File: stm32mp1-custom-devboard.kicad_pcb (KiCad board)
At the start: 2 copper layers, 120 x 72 mm, 16 parts, among them Con1 52746-0671, Con2 505110-2491, P1 FH12A-30S-0.5SH(55), U1 TPS61169DCKR, U2 MCP1703T-3302E

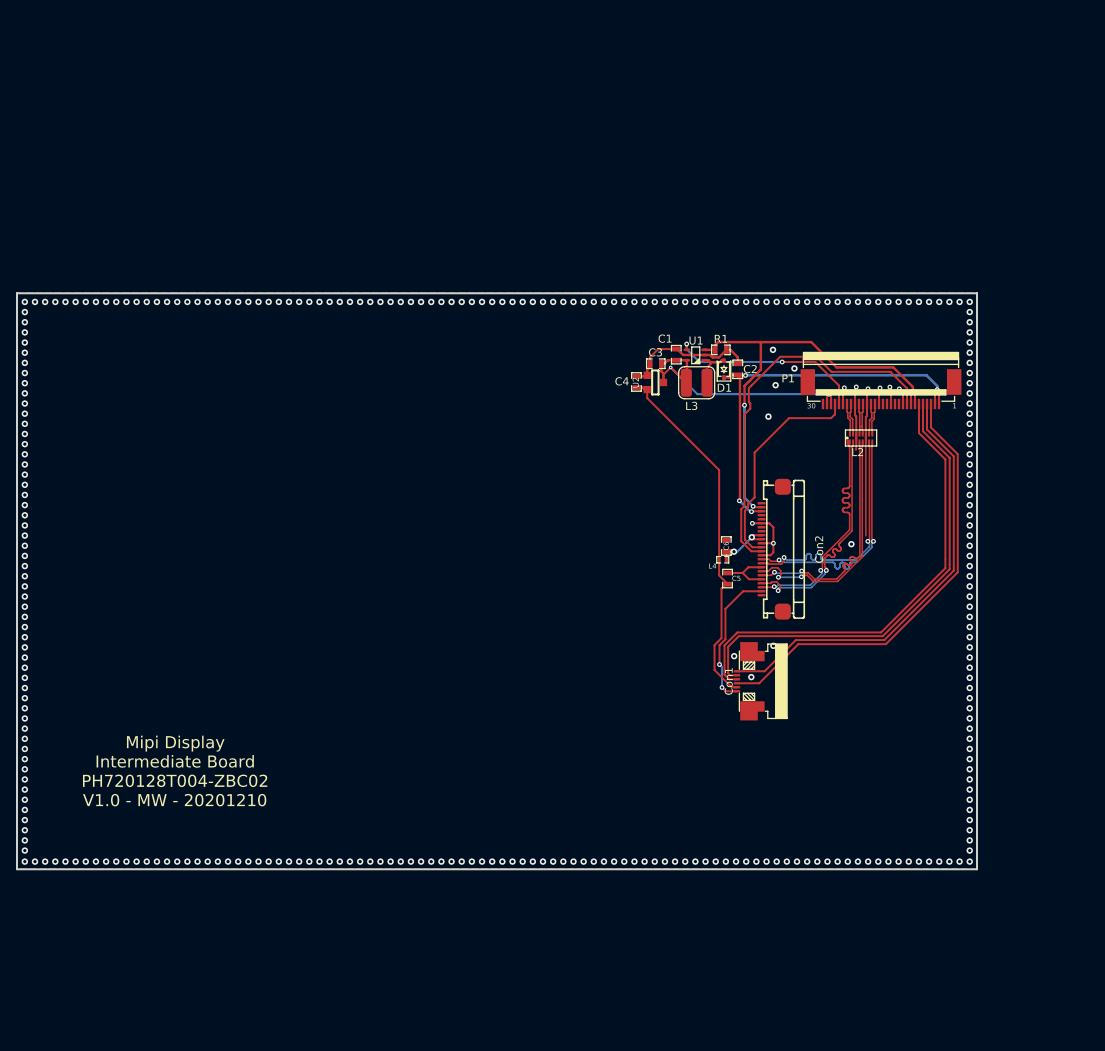
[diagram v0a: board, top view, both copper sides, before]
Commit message: Added stm32mp1 module and arduino shield
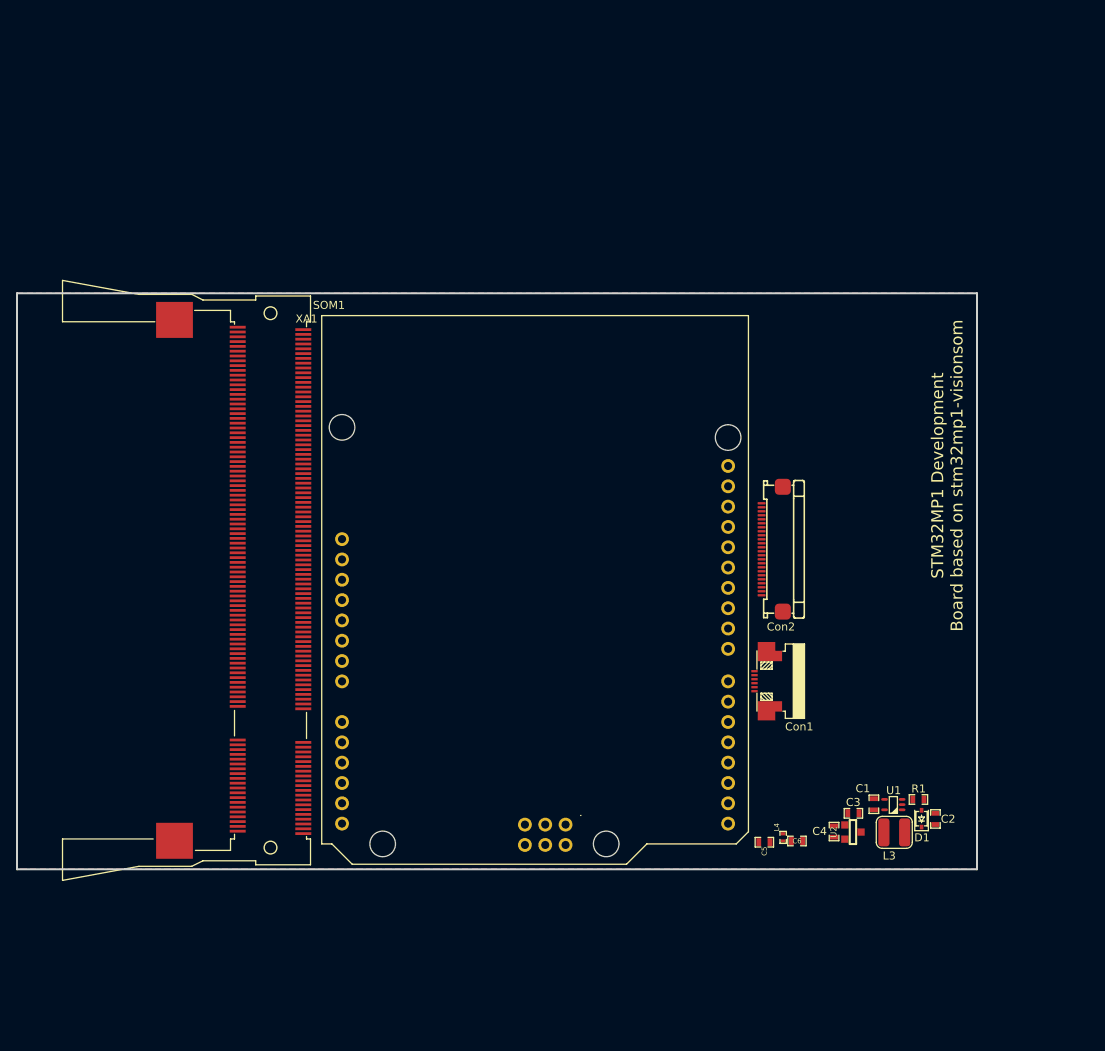
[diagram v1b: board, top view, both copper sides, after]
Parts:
- removed L2: EMI8133MUTAG, Inductors:EMI8133MUTAG
- removed P1: FH12A-30S-0.5SH(55), Fpc_Connectors:FH12A-30S-0.5SH
- added SOM1: VisionSOM-STM32MP1, SomLabs_SOM:VisionSOM-STM32MP1, F.Cu at (124.8, 102.3)
- added XA1: Arduino_101_Shield, Arduino:Arduino_101_Shield, F.Cu at (131.2, 69.2)
- moved D1 61.4 mm to (206.2, 132.1)
- moved U2 61.4 mm to (197.6, 133.8)
- moved C1 61.4 mm to (200.2, 130.3)
- moved C2 61.4 mm to (207.9, 132.1)
- moved C4 61.4 mm to (195.2, 133.7)
- moved L3 61.4 mm to (202.8, 133.8)
- moved R1 61.4 mm to (205.8, 129.7)
- moved U1 61.4 mm to (202.7, 130.3)
- moved C3 61.4 mm to (197.7, 131.4)
- moved C6 37.9 mm to (190.6, 134.9), turned to 0 degrees
- moved L4 35.5 mm to (188.9, 134.4), turned to 90 degrees
- moved C5 33.3 mm to (186.5, 135.0), turned to 0 degrees
- moved Con1 2.19 mm to (187.3, 114.9)
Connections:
- Con1 pad 3: /LCD+Touchscreen common connector/TP_NT -> (no net)
- Con1 pad 4: /LCD+Touchscreen common connector/TP_SDA -> (no net)
- Con1 pad 5: /LCD+Touchscreen common connector/TP_SCL -> (no net)
- Con1 pad 6: /LCD+Touchscreen common connector/TP_RESET -> (no net)
- Con2 pad 12: /LCD+Touchscreen common connector/LCD_RESET -> (no net)
- Con2 pad 13: /LCD+Touchscreen common connector/LCD_TE -> (no net)
- Con2 pad 15: /LCD+Touchscreen/MIPI_CLK+ -> (no net)
- Con2 pad 16: /LCD+Touchscreen/MIPI_CLK- -> (no net)
- Con2 pad 18: /LCD+Touchscreen/MIPI_D1+ -> (no net)
- Con2 pad 19: /LCD+Touchscreen/MIPI_D1- -> (no net)
- Con2 pad 21: /LCD+Touchscreen/MIPI_D0+ -> (no net)
- Con2 pad 22: /LCD+Touchscreen/MIPI_D0- -> (no net)
- U1 pad 4: /LCD+Touchscreen common connector/LCD_BACKLIGHT_PWM -> (no net)
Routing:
- net GND: track 86.2 -> 0.00 mm, vias 314 -> 0
- net /LCD+Touchscreen/LCD_LED-: track 81.2 -> 0.00 mm, vias 3 -> 0
- net /LCD+Touchscreen common connector/TP_SDA: track 59.0 -> 0.00 mm
- net /LCD+Touchscreen common connector/TP_SCL: track 58.3 -> 0.00 mm
- net /LCD+Touchscreen common connector/TP_NT: track 55.8 -> 0.00 mm
- net /LCD+Touchscreen common connector/TP_RESET: track 54.5 -> 0.00 mm
- net /LCD+Touchscreen/LCD_LED+: track 51.5 -> 0.00 mm, vias 4 -> 0
- net /LCD+Touchscreen common connector/LCD_TE: track 47.7 -> 0.00 mm
- net /LCD+Touchscreen/Touchscreen Power Supply/VOUT_3.3V_250mA: track 45.2 -> 0.00 mm
- net VDD: track 37.5 -> 0.00 mm, vias 2 -> 0
- net /LCD+Touchscreen/MIPI_CLK-: track 30.4 -> 0.00 mm, vias 2 -> 0
- net /LCD+Touchscreen/MIPI_CLK+: track 30.4 -> 0.00 mm, vias 2 -> 0
- net /LCD+Touchscreen/MIPI_D1-: track 30.2 -> 0.00 mm, vias 2 -> 0
- net /LCD+Touchscreen/MIPI_D0+: track 30.2 -> 0.00 mm, vias 2 -> 0
- net /LCD+Touchscreen/MIPI_D1+: track 30.2 -> 0.00 mm, vias 2 -> 0
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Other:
- board text added: "STM32MP1 Development Board based on stm32mp1-visionsom"
- board text removed: "Mipi Display Intermediate Board PH720128T004-ZBC02 V1.0 - MW - 20201210"

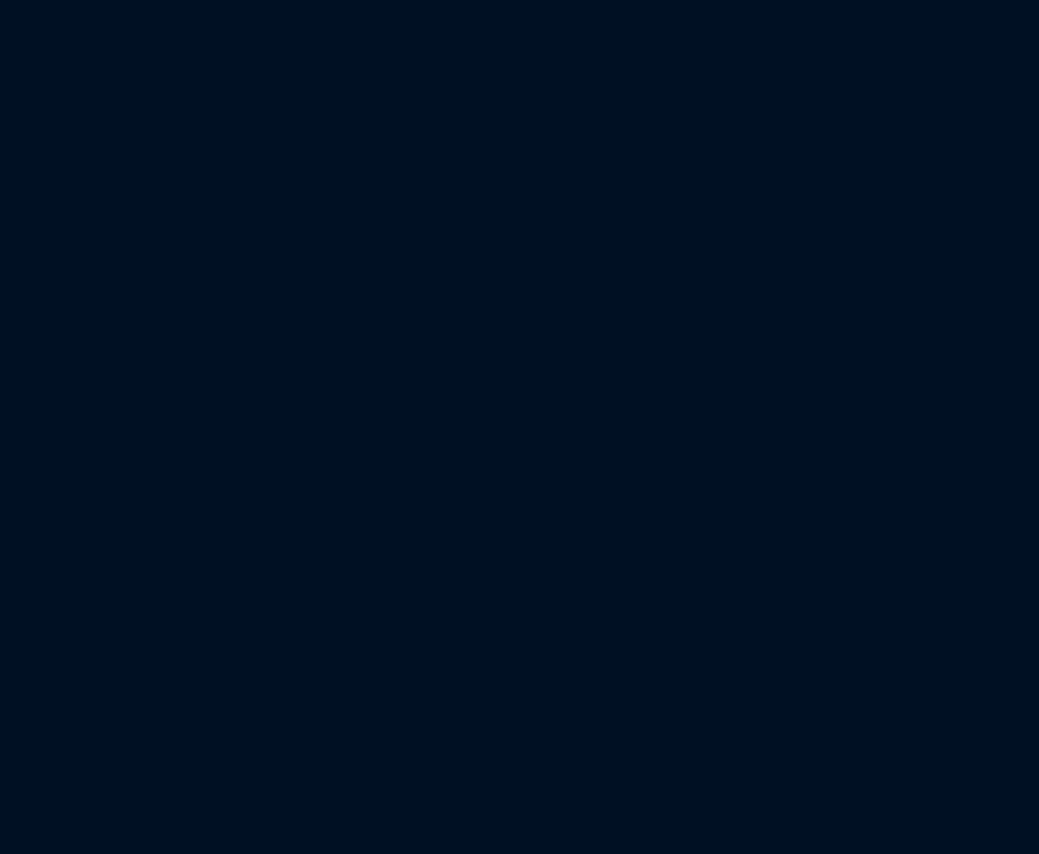
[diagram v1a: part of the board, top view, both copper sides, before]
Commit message: Added new components and hierarchical sheets
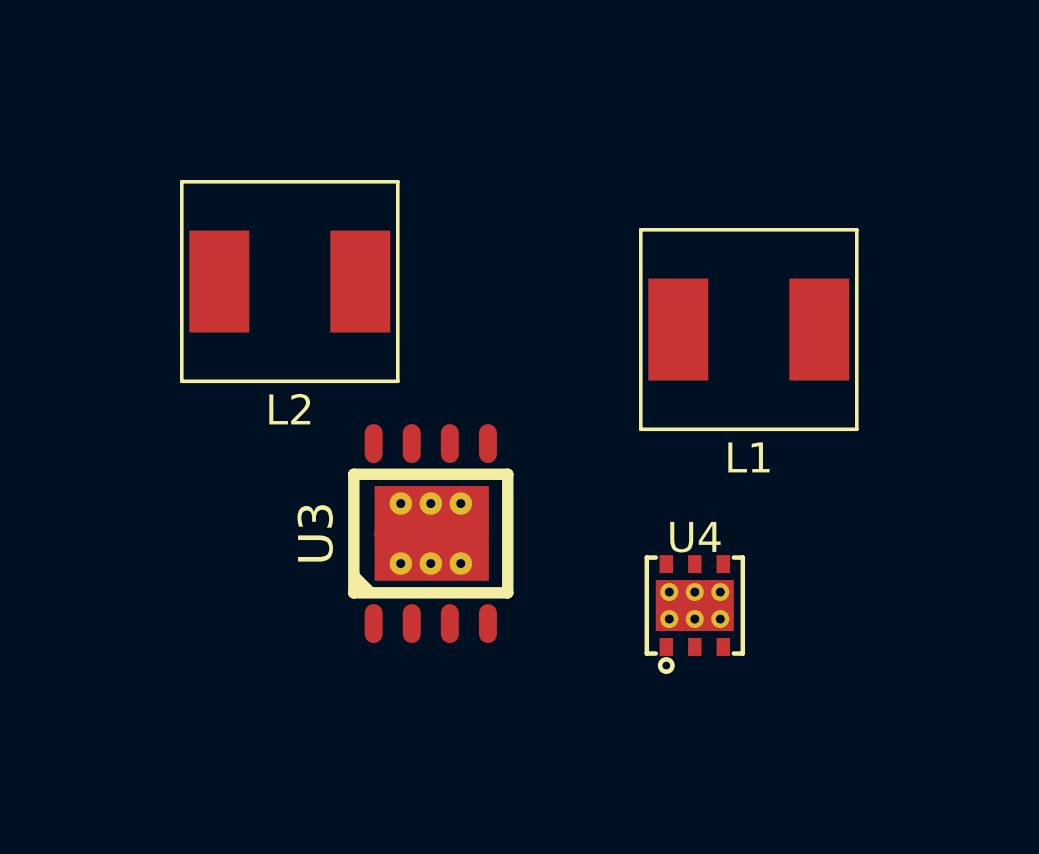
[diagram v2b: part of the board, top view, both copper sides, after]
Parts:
- added L1: 3.3uH-13.5A-ASPI-0630HI-3R3M-T15, Inductors:ASPI-0630HI-3R3M-T15, F.Cu at (163.4, 112.9)
- added L2: 3.3uH-13.5A-ASPI-0630HI-3R3M-T15, Inductors:ASPI-0630HI-3R3M-T15, F.Cu at (148.1, 111.3)
- added U3: ST1S10PHR, Switching:ST1S10PHR_SOIC8, F.Cu at (152.8, 119.7)
- added U4: ST1S09IPUR, Switching:ST1S09IPUR, F.Cu at (161.6, 122.1)
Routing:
- added copper zone on In2.Cu, net GND
- added copper zone on In1.Cu, net VDD
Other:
- copper layers 2 -> 4

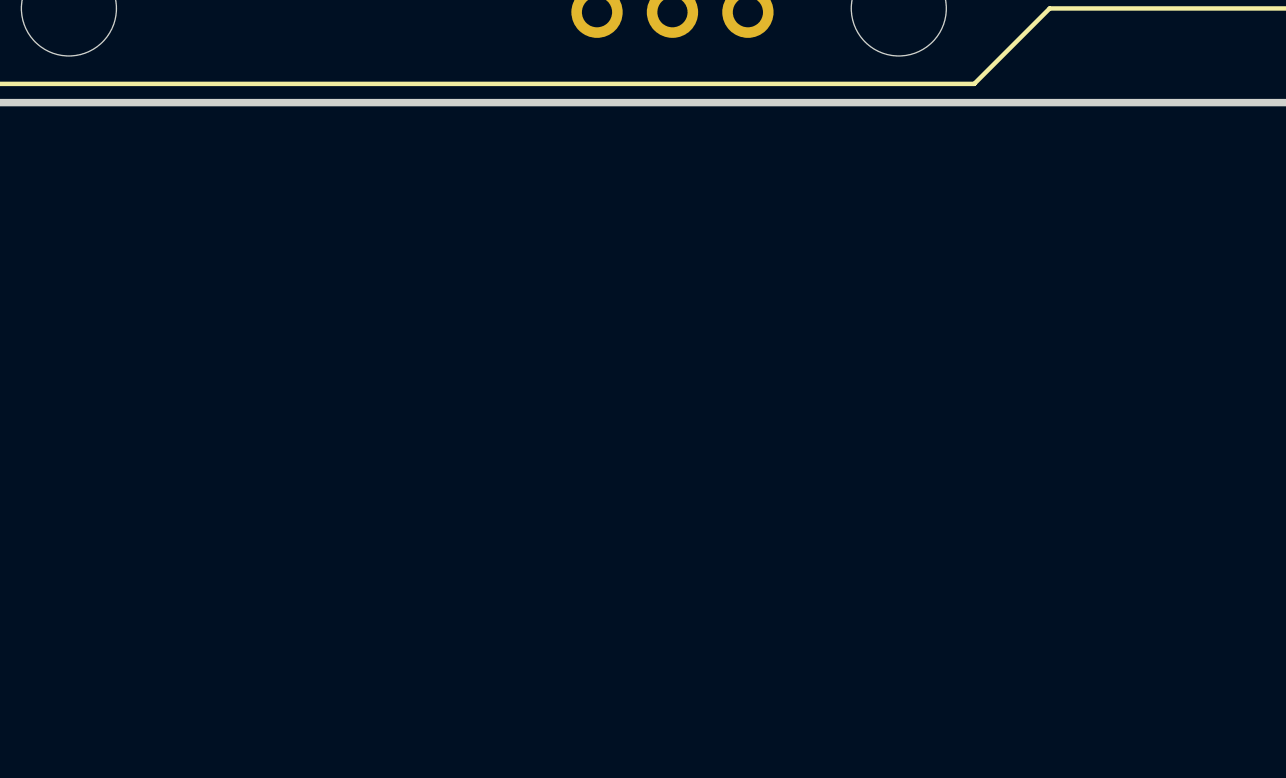
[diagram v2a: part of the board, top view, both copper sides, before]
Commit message: Added power source module
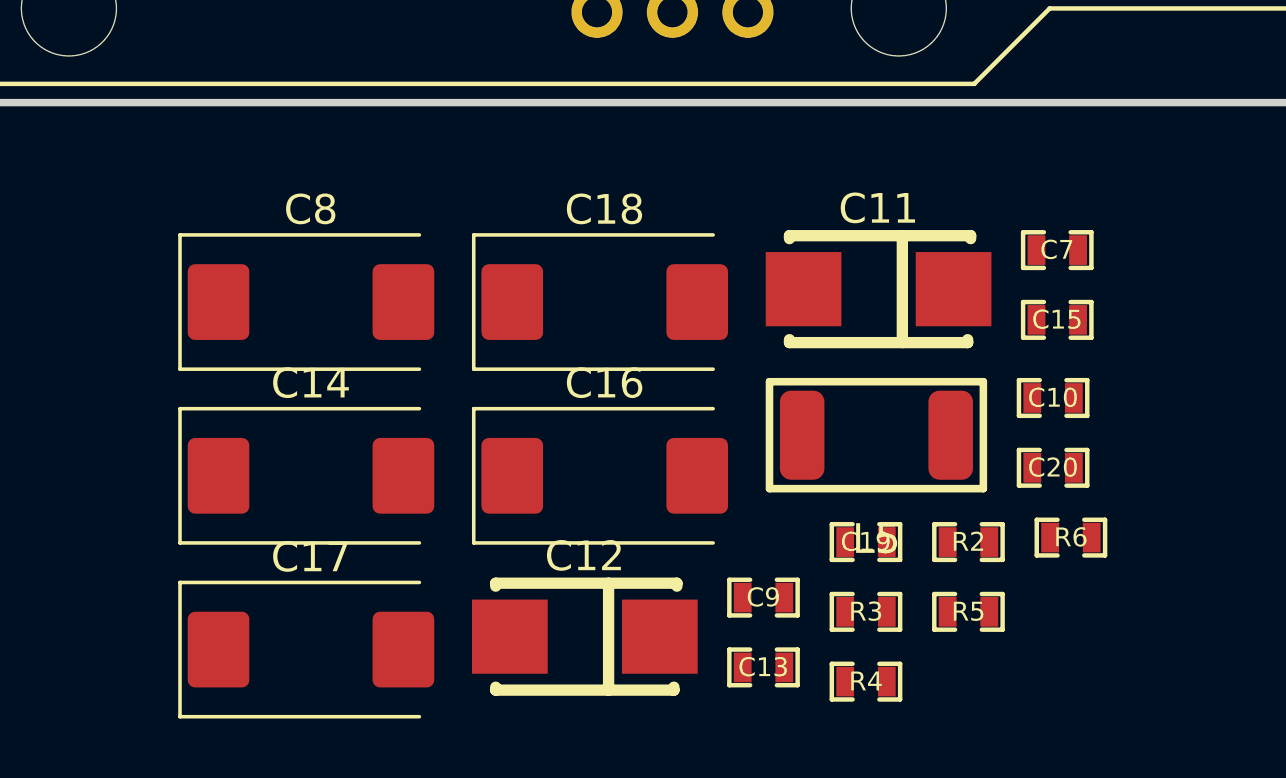
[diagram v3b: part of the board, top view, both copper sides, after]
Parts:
- added C10: 100nF/50V, Capacitors_Smd_0603:100nF_0603, F.Cu at (172.0, 148.4)
- added C11: 10uF/35V, Smd_Tantal:10uF_35V_C, F.Cu at (166.1, 144.7)
- added C12: 10uF/35V, Smd_Tantal:10uF_35V_C, F.Cu at (156.2, 156.4)
- added C13: 100nF/50V, Capacitors_Smd_0603:100nF_0603, F.Cu at (162.2, 157.4)
- added C14: 22uF35V, Smd_Tantal:22uF_35V_Size_D, F.Cu at (147.0, 151.0)
- added C15: 10nF/50V, Capacitors_Smd_0603:10nF_0603, F.Cu at (172.1, 145.7)
- added C16: 22uF35V, Smd_Tantal:22uF_35V_Size_D, F.Cu at (156.9, 151.0)
- added C17: 22uF35V, Smd_Tantal:22uF_35V_Size_D, F.Cu at (147.0, 156.8)
- added C18: 22uF35V, Smd_Tantal:22uF_35V_Size_D, F.Cu at (156.9, 145.1)
- added C19: 100nF/50V, Capacitors_Smd_0603:100nF_0603, F.Cu at (165.7, 153.2)
- added C20: 100nF/50V, Capacitors_Smd_0603:100nF_0603, F.Cu at (172.0, 150.7)
- added C7: 100nF/50V, Capacitors_Smd_0603:100nF_0603, F.Cu at (172.1, 143.4)
- added C8: 22uF35V, Smd_Tantal:22uF_35V_Size_D, F.Cu at (147.0, 145.1)
- added C9: 100nF/50V, Capacitors_Smd_0603:100nF_0603, F.Cu at (162.2, 155.1)
- added L5: 742792515, Inductors:742792515, F.Cu at (166.0, 149.6)
- added R2: 2k,1%, Resistor_Smd_0603:2k_0603, F.Cu at (169.1, 153.2)
- added R3: 68k, Resistor_Smd_0603:68k_0603, F.Cu at (165.7, 155.6)
- added R4: 21k, Resistor_Smd_0603:21k_0603, F.Cu at (165.7, 157.9)
- added R5: 11k,1%, Resistor_Smd_0603:11k_0603, F.Cu at (169.1, 155.6)
- added R6: 2k,1%, Resistor_Smd_0603:2k_0603, F.Cu at (172.6, 153.1)
- L1, L2: value 3.3uH-13.5A-ASPI-0630HI-3R3M-T15 -> 3.3uH-13.5A
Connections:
- L1 pad 1: (no net) -> Net-(L1-Pad1)
- L1 pad 2: (no net) -> /Power Supply Module/POWER_OUT_5V_3A
- L2 pad 1: (no net) -> Net-(L2-Pad1)
- L2 pad 2: (no net) -> /Power Supply Module/POWER_OUT_3V3_2A
- U3 pad 0: Net-(U3-Pad0) -> GND
- U3 pad 1: (no net) -> Net-(C10-Pad1)
- U3 pad 2: (no net) -> Net-(R2-Pad2)
- U3 pad 3: (no net) -> Net-(C15-Pad2)
- U3 pad 4: (no net) -> GND
- U3 pad 5: (no net) -> GND
- U3 pad 6: (no net) -> Net-(C10-Pad1)
- U3 pad 7: (no net) -> Net-(L1-Pad1)
- U3 pad 8: (no net) -> GND
- U4 pad 1: (no net) -> Net-(R3-Pad2)
- U4 pad 3: (no net) -> Net-(L2-Pad1)
- U4 pad 4: (no net) -> /Power Supply Module/POWER_IN_7_TO_18V
- U4 pad 5: (no net) -> /Power Supply Module/POWER_IN_7_TO_18V
- U4 pad 6: (no net) -> /Power Supply Module/POWER_IN_7_TO_18V
